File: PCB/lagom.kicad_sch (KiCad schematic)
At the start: 156 parts, among them J1 Conn_01x04, J2 Conn_01x03, SW83 RotaryEncoder_Switch, SW84 RotaryEncoder_Switch, U1 ProMicro, U2 74HC138, U3 74HC138

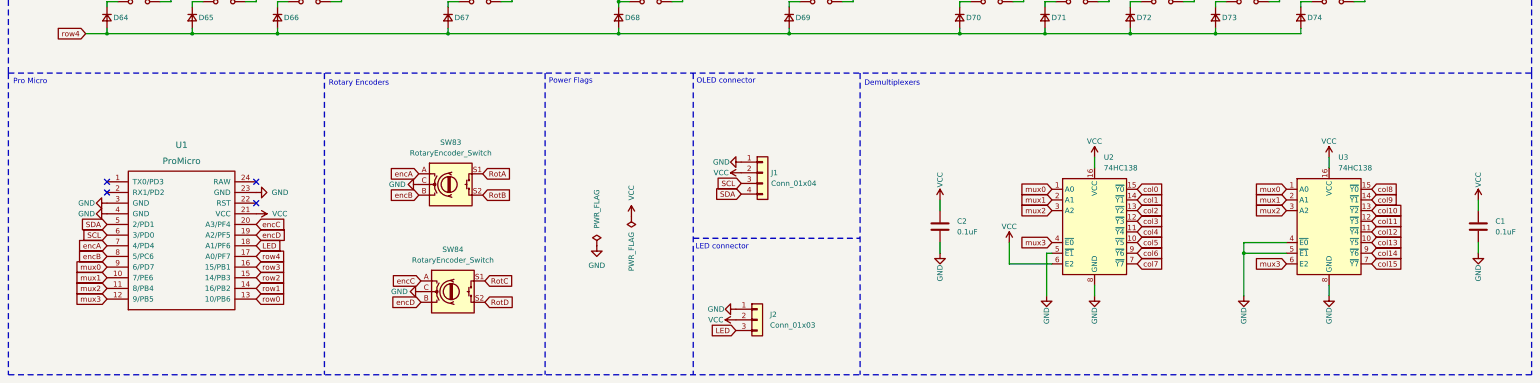
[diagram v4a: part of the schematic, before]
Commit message: Add battery connector, reset and power switch to schematic
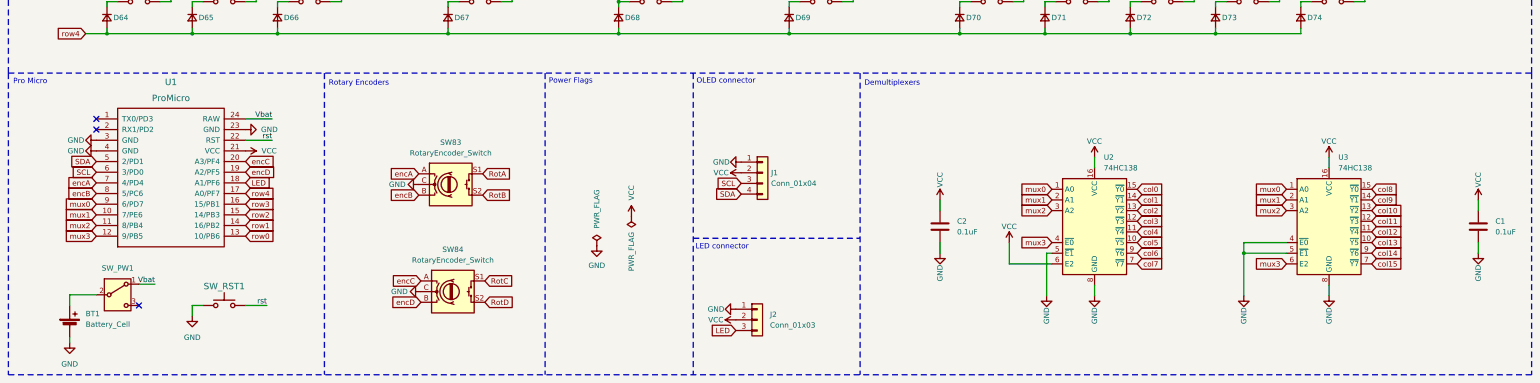
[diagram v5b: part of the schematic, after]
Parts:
- added BT1: Battery_Cell, Connector_JST:JST_PH_S2B-PH-K_1x02_P2.00mm_Horizontal, symbol Device:Battery_Cell
- added SW_PW1: SW_SPDT, Connector_PinHeader_2.54mm:PinHeader_1x03_P2.54mm_Vertical, symbol Switch:SW_SPDT
- added SW_RST1: KEYSW, Button_Switch_THT:SW_PUSH_1P1T_6x3.5mm_H5.0_APEM_MJTP1250, symbol Switch:SW_Push
- D1: footprint Diode_THT:D_DO-34_SOD68_P7.62mm_Horizontal -> Button_Switch_THT:SW_PUSH_1P1T_6x3.5mm_H5.0_APEM_MJTP1250
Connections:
- net GND: now also BT1.2 (-), SW_RST1.1
- net rst: now reaches U1.22 (RST)
- net rst: now also SW_RST1.2
- net Vbat: now reaches U1.24 (RAW)
- net Vbat: now also SW_PW1.1 (A)
- new net: BT1.1 (+), SW_PW1.2 (B)
- no-connect marks 6 -> 5
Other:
- moved on the sheet: U1

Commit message: All Diodes 1N4148 type
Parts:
- D1, D10, D11, D12, D13, D14, D15, D16, D17, D18, D19, D2, D20, D21, D22, D23, D24, D25, D26, D27, D28, D29, D3, D30, D31, D32, D33, D34, D35, D36, D37, D38, D39, D4, D40, D41, D42, D43, D44, D45, D46, D47, D48, D49, D5, D50, D51, D52, D53, D54, D55, D56, D57, D58, D59, D6, D60, D61, D62, D63, D64, D65, D66, D67, D68, D69, D7, D70, D71, D72, D73, D74, D8, D9: value D_Small -> 1N4148
- SW_RST1: MPN CST35605T -> (none)

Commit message: Capacitor fp -> 0805
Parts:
- C1, C2: footprint Capacitor_THT:C_Disc_D4.7mm_W2.5mm_P5.00mm -> Capacitor_SMD:C_0805_2012Metric
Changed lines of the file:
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@@
 			)
 		)
-		(property "Footprint" "Capacitor_THT:C_Disc_D4.7mm_W2.5mm_P5.00mm"
+		(property "Footprint" "Capacitor_SMD:C_0805_2012Metric"
 			(at 252.8062 197.104 0)
 			(effects
@@
 			)
 		)
-		(property "Footprint" "Capacitor_THT:C_Disc_D4.7mm_W2.5mm_P5.00mm"
+		(property "Footprint" "Capacitor_SMD:C_0805_2012Metric"
 			(at 381.0762 197.104 0)
 			(effects

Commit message: main schematic: Change switch footprints to hotswap, add custom switch fp library
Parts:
- SW_/1, SW_0, SW_1, SW_2, SW_3, SW_4, SW_5, SW_6, SW_7, SW_8, SW_9, SW_A1, SW_B1, SW_C1, SW_COMMA1, SW_D1, SW_DOT1, SW_DOWN1, SW_E1, SW_ENC1, SW_ENC2, SW_END1, SW_EQUAL1, SW_ESC1, SW_F1, SW_G1, SW_H1, SW_HOME1, SW_I1, SW_ISO_\1, SW_ISO_`1, SW_J1, SW_K1, SW_L1, SW_LEFT1, SW_LSQBR1, SW_M1, SW_MINUS1, SW_N1, SW_O1, SW_P1, SW_PGDN1, SW_PGUP1, SW_Q1, SW_QUOTE1, SW_R1, SW_RIGHT1, SW_RSQBR1, SW_S1, SW_SEMICOLON1, SW_T1, SW_U1, SW_UP1, SW_V1, SW_W1, SW_X1, SW_Y1, SW_Z1: footprint Button_Switch_Keyboard:SW_Cherry_MX_1.00u_PCB -> kailh_hotswap:SW_Kailh_HotSwap_1.00u_PCB
- SW_6.25U_SPACE1: footprint Button_Switch_Keyboard:SW_Cherry_MX_6.25u_PCB -> kailh_hotswap:SW_Kailh_HotSwap_6.25u_PCB
- SW_BCKSP1: footprint Button_Switch_Keyboard:SW_Cherry_MX_2.00u_PCB -> kailh_hotswap:SW_Kailh_HotSwap_2.00u_PCB
- SW_CAPS1, SW_RSHIFT1: footprint Button_Switch_Keyboard:SW_Cherry_MX_1.75u_PCB -> kailh_hotswap:SW_Kailh_HotSwap_1.75u_PCB
- SW_ISO_ENT1: footprint Button_Switch_Keyboard:SW_Cherry_MX_ISOEnter_PCB_Flipped_Rotated -> kailh_hotswap:SW_Kailh_HotSwap_ISOEnter_PCB
- SW_ISO_LSHF1, SW_LALT_1.25U1, SW_LCMD_1.25U1, SW_LCTRL_1.25U1, SW_R_CMD1, SW_R_CTRL_1.25U1, SW_SPL_SPACE_M1: footprint Button_Switch_Keyboard:SW_Cherry_MX_1.25u_PCB -> kailh_hotswap:SW_Kailh_HotSwap_1.25u_PCB
- SW_SPL_SPACE_L1: footprint Button_Switch_Keyboard:SW_Cherry_MX_2.25u_PCB -> kailh_hotswap:SW_Kailh_HotSwap_2.25u_PCB
- SW_SPL_SPACE_R1: footprint Button_Switch_Keyboard:SW_Cherry_MX_2.75u_PCB -> kailh_hotswap:SW_Kailh_HotSwap_2.75u_PCB
- SW_TAB1: footprint Button_Switch_Keyboard:SW_Cherry_MX_1.50u_Plate -> kailh_hotswap:SW_Kailh_HotSwap_1.50u_PCB
